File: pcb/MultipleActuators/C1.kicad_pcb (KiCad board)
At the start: 2 copper layers, 98.5 x 59.3 mm, 26 parts, among them J1 Screw_Terminal_01x02, J12 Screw_Terminal_01x03, J2 Screw_Terminal_01x02, J3 Screw_Terminal_01x02, J4 Screw_Terminal_01x02, J5 Screw_Terminal_01x02, J6 Screw_Terminal_01x02, J7 Screw_Terminal_01x02, Q1 BT136-500, Q2 BT136-500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

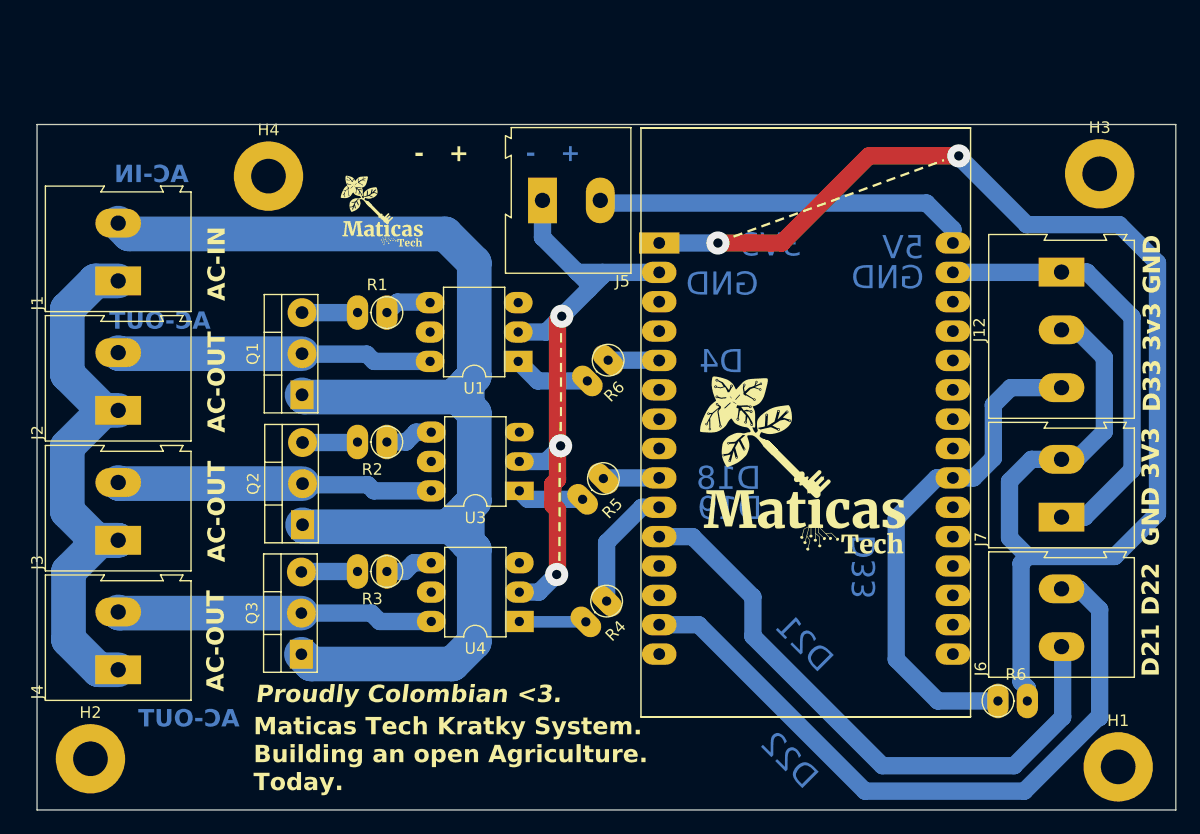
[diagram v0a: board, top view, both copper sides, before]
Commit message: Update
now this adds the HLK-PM01 so that this can have it's own AC-DC adapter built in, and has way more comfortable connection cable management inside a box. Next iterations will be replacing the connectors for the SDA and SCL (and all those 7 signal pins) for more robust and compact ones. In this iteration the sizing of the AC traces were all changed to match a 3mm width which allows for 5A input current handling at most, with a delta of 10°C.
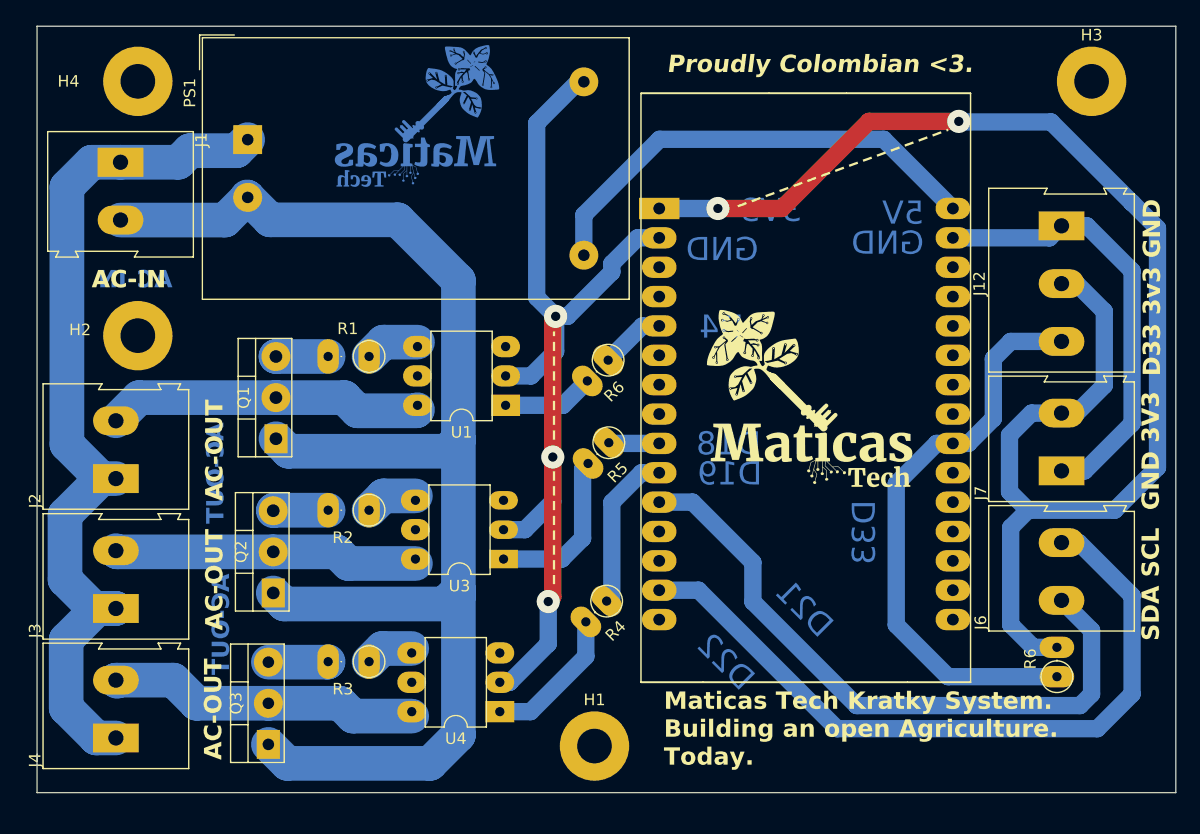
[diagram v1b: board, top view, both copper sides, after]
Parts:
- removed J5: Screw_Terminal_01x02, TerminalBlock:TerminalBlock_Altech_AK300-2_P5.00mm
- added PS1: HLK-PM01, Converter_ACDC:Converter_ACDC_Hi-Link_HLK-PMxx, F.Cu at (90.5, 50.0)
- moved H1 45.3 mm to (120.5, 102.5)
- moved H2 36.8 mm to (81.0, 67.0)
- moved H4 14.0 mm to (81.0, 45.0)
- moved J1 10.3 mm to (79.5, 52.0), turned to -90 degrees
- moved Q3 8.31 mm to (92.3, 101.3)
- moved R3 8.20 mm to (100.0, 95.2)
- moved H3 8.03 mm to (163.5, 45.0)
- moved U4 7.98 mm to (112.3, 99.5)
- moved R2 6.42 mm to (100.0, 82.1)
- moved Q2 6.42 mm to (92.7, 88.2)
- moved U3 6.06 mm to (112.6, 86.3)
- moved J2 5.90 mm to (79.1, 79.4)
- moved J3 5.90 mm to (79.1, 90.6)
- moved J4 5.90 mm to (79.1, 101.8)
- moved R6 5.52 mm to (160.5, 96.5), turned to 90 degrees
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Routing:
- net GND: track 96.6 -> 127.3 mm
- net AC2: track 48.9 -> 77.2 mm
- net AC1: track 115.6 -> 124.6 mm
- net Net-(R5-Pad2): track 5.78 -> 14.3 mm
- net 5V: track 33.1 -> 40.6 mm
- net Net-(R4-Pad2): track 5.87 -> 12.6 mm
- net D33: track 43.2 -> 49.4 mm
- net D22: track 61.1 -> 64.6 mm
- net D21: track 53.0 -> 56.3 mm
- net D19: track 10.9 -> 13.7 mm
- net 3V3: track 126.9 -> 128.2 mm
- net Net-(R6-Pad2): track 6.68 -> 7.95 mm
- net D4: track 4.51 -> 5.76 mm
- net Net-(J3-Pin_2): track 27.4 -> 26.4 mm
- net Net-(R1-Pad1): track 4.13 -> 4.77 mm
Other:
- board size 98.5 x 59.3 mm -> 98.5 x 66.3 mm
- board text added: "SDA SCL"
- board text removed: "- +"
- board text removed: "D21 D22"
